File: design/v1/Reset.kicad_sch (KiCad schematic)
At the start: 12 parts, among them IC15 555N

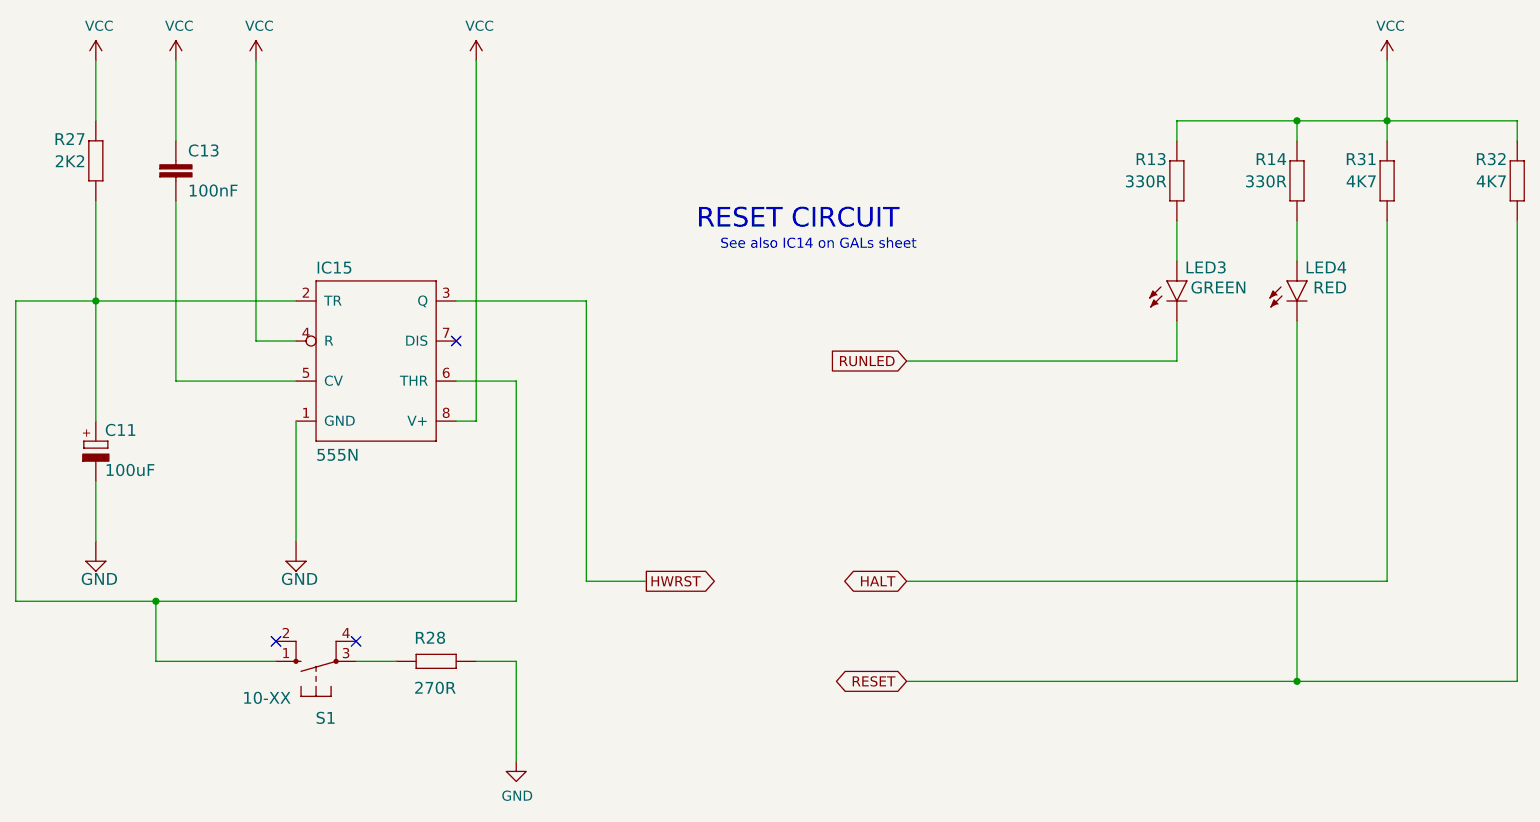
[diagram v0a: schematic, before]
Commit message: First program of the ATF1508
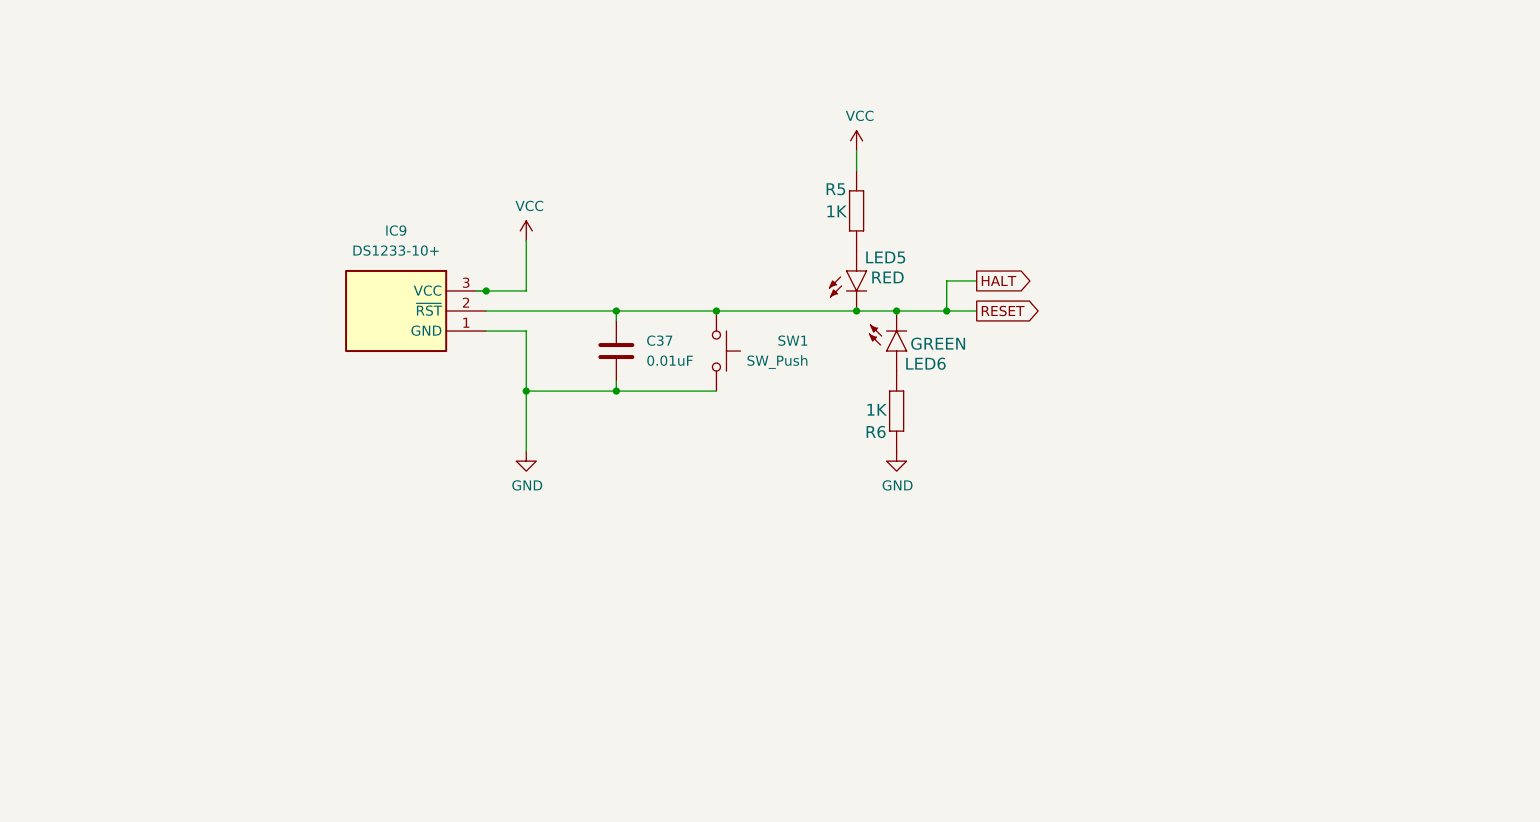
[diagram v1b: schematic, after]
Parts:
- removed C11: 100uF, rosco_m68k:E2,5-5, symbol rosco_m68k-eagle-import:CPOL-EUE2.5-5
- removed C13: 100nF, rosco_m68k:C2.5-3, symbol rosco_m68k-eagle-import:C2,5-3
- removed IC15: 555N, Package_DIP:DIP-8_W7.62mm_LongPads, symbol rosco_m68k-eagle-import:555N
- removed LED3: GREEN, rosco_m68k:LED5MM, symbol rosco_m68k-eagle-import:LED5MM
- removed LED4: RED, rosco_m68k:LED5MM, symbol rosco_m68k-eagle-import:LED5MM
- removed R13, R14: 330R, rosco_m68k:0207_10, symbol rosco_m68k-eagle-import:R-EU_0207_10
- removed R27: 2K2, rosco_m68k:0207_10, symbol rosco_m68k-eagle-import:R-EU_0207_10
- removed R28: 270R, rosco_m68k:0207_10, symbol rosco_m68k-eagle-import:R-EU_0207_10
- removed R31, R32: 4K7, rosco_m68k:0207_10, symbol rosco_m68k-eagle-import:R-EU_0207_10
- removed S1: 10-XX, rosco_m68k:B3F-10XX, symbol rosco_m68k-eagle-import:10-XX
- added C37: 0.01uF, symbol Device:C
- added IC9: DS1233-10+, TO-92, symbol DS1233:DS1233-10+
- added LED5: RED, rosco_m68k:LED5MM, symbol rosco_m68k-eagle-import:LED5MM
- added LED6: GREEN, rosco_m68k:LED5MM, symbol rosco_m68k-eagle-import:LED5MM
- added R5, R6: 1K, rosco_m68k:0207_10, symbol rosco_m68k-eagle-import:R-EU_0207_10
- added SW1: SW_Push, symbol Switch:SW_Push
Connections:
- net GND: now also C37.2, IC9.1 (GND), R6.2, SW1.1
- net HALT: now also C37.1, IC9.2 (~{RST}), LED5.K (C), LED6.K (C), SW1.2
- net VCC: now also IC9.3 (VCC), R5.2
- new net: LED6.A, R6.1
- new net: LED5.A, R5.1
- no-connect marks 3 -> 0
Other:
- note removed: "RESET CIRCUIT"
- note removed: "See also IC14 on GALs sheet"

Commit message: Tidy up readme
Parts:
- C37: footprint (none) -> rosco_m68k:C2.5-3
- SW1: footprint (none) -> rosco_m68k:B3F-10XX
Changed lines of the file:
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@@
 			)
 		)
-		(property "Footprint" ""
+		(property "Footprint" "rosco_m68k:B3F-10XX"
 			(at 135.89 92.71 0)
 			(effects
@@
 			)
 		)
-		(property "Footprint" ""
+		(property "Footprint" "rosco_m68k:C2.5-3"
 			(at 119.0752 96.52 0)
 			(effects
